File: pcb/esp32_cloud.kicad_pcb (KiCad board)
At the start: 2 copper layers, 50 x 30.9 mm, 23 parts, among them J1 Conn_01x04_Male, J2 Conn_01x03_Male, J3 USB_C_Receptacle_USB2.0, J4 Conn_01x06_Male, J5 Conn_01x10_Male, J6 Conn_01x03_Male, U1 ESP32-PICO-D4, U2 AN91445, U3 XC6220B331MR

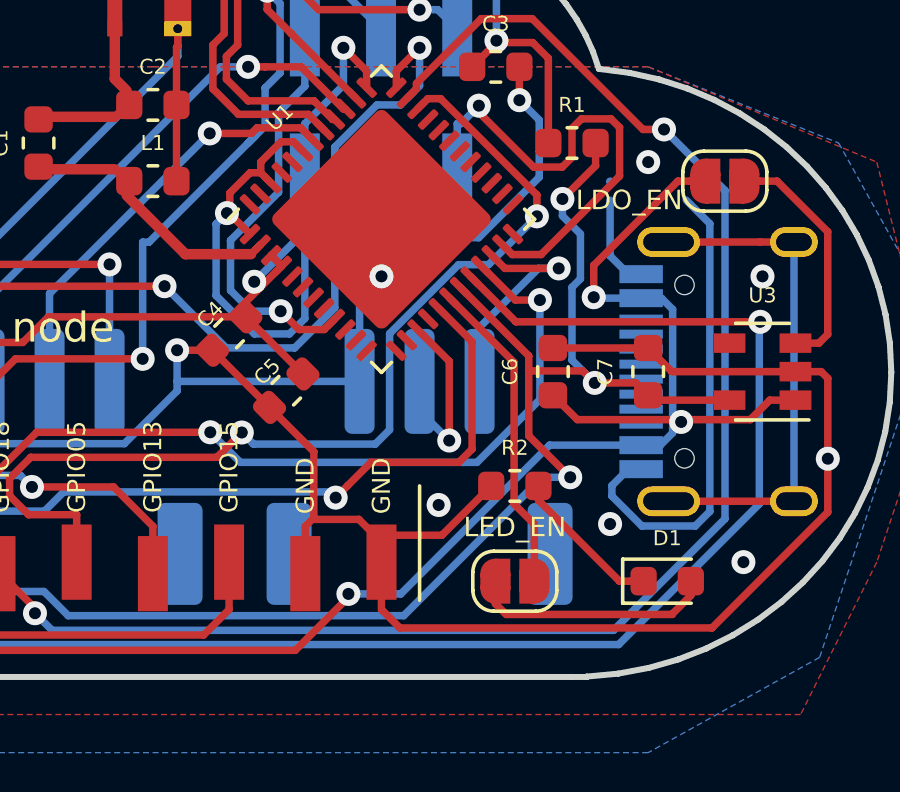
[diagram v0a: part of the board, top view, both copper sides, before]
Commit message: J6 changed from ADC2 to ADC1 GPIOs
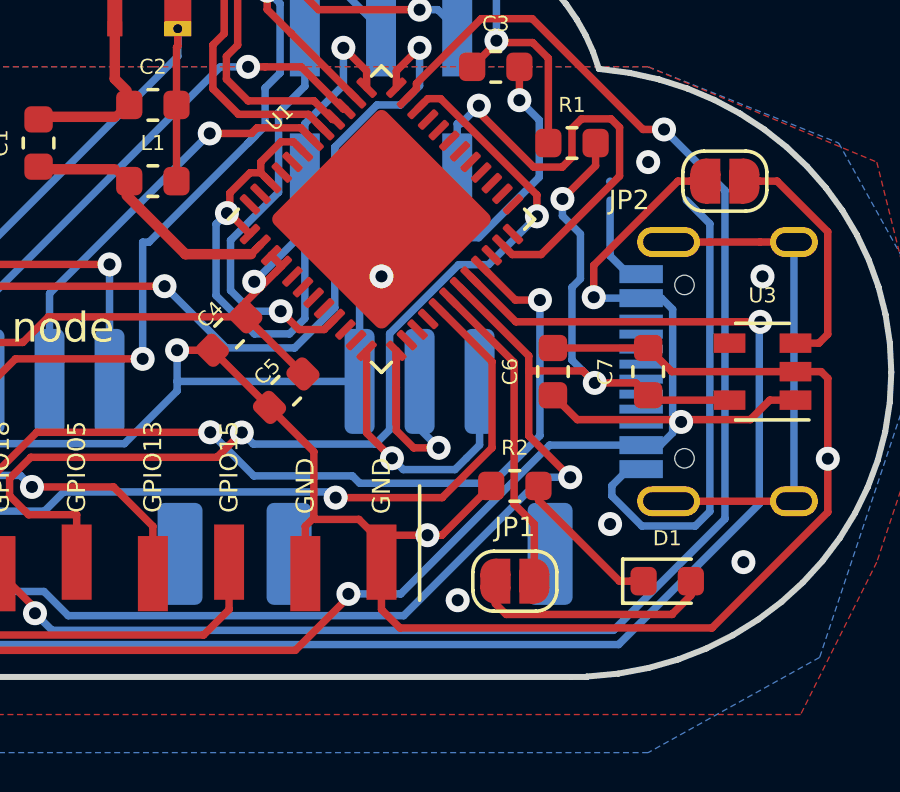
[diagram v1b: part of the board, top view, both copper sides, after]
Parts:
- renumbered LED_EN to JP1, LDO_EN to JP2
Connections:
- J6 pad 1: /WS2812_VCC -> /GPIO32
- J6 pad 2: /WS2812_DATA -> /GPIO33
- U1 pad 12: Net-(U1-Pad12) -> /GPIO32
- U1 pad 13: Net-(U1-Pad13) -> /GPIO33
- U1 pad 15: /WS2812_DATA -> Net-(U1-Pad15)
- U1 pad 22: /WS2812_VCC -> Net-(U1-Pad22)
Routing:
- net /GPIO33: track 0.00 -> 10.2 mm, vias 0 -> 1
- net /GPIO32: track 0.00 -> 9.47 mm, vias 0 -> 1
- net /WS2812_VCC: track 7.67 -> 0.00 mm, vias 1 -> 0
- net /WS2812_DATA: track 6.52 -> 0.00 mm, vias 1 -> 0
- net /GPIO15_ADC2_CH3: track 41.4 -> 42.7 mm
- net /BME280_VCC: track 59.6 -> 60.5 mm
- net GND: vias 11 -> 12
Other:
- board text added: "board rev 1.2"
- board text removed: "board rev 1.1"
